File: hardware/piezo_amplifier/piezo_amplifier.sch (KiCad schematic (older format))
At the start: 4 parts

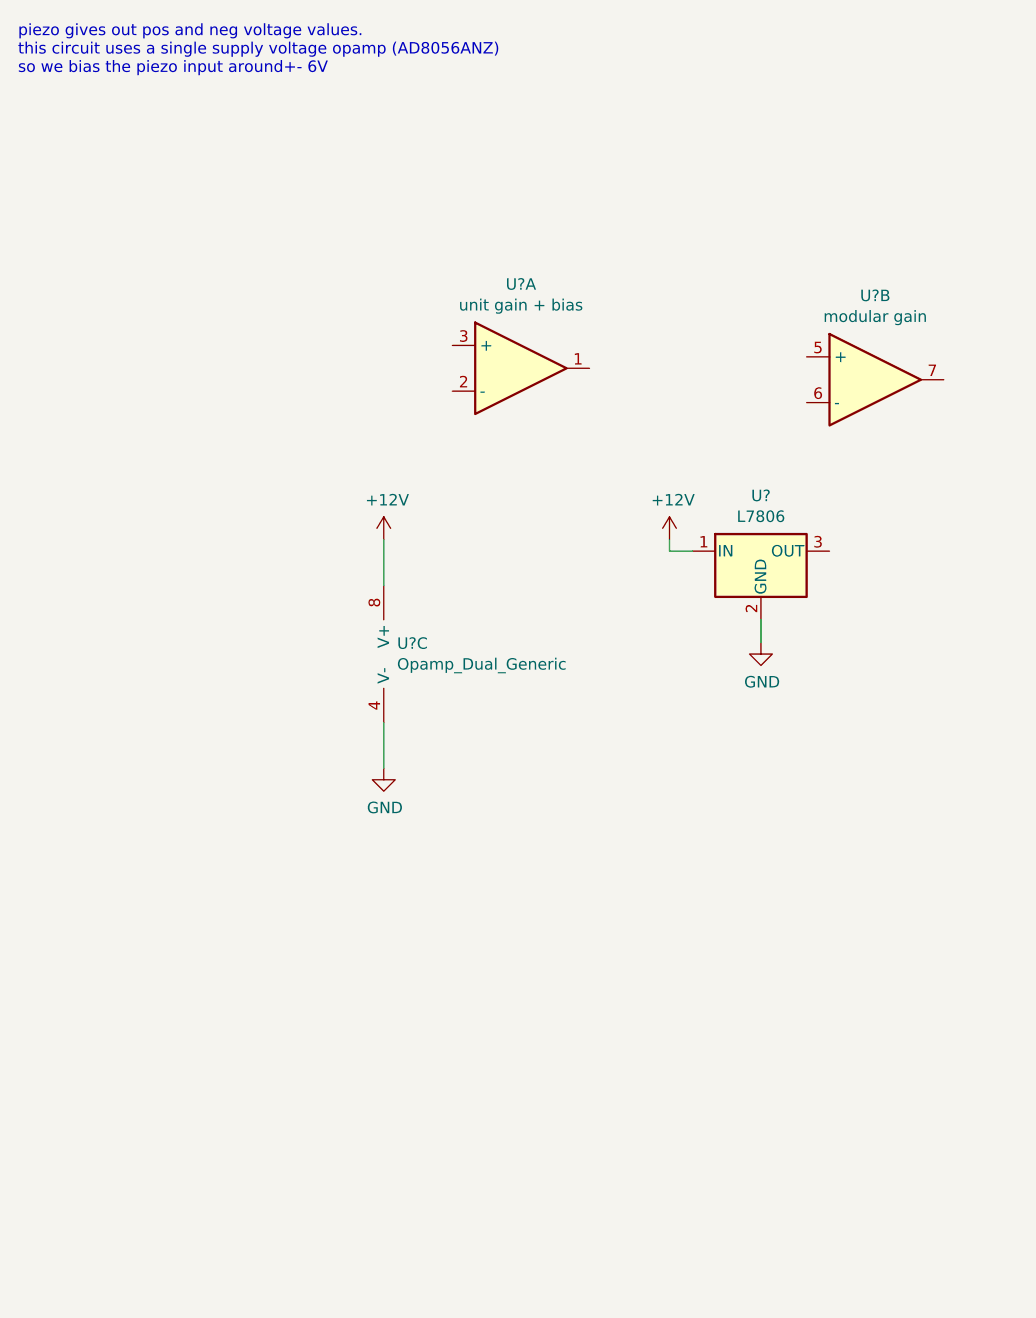
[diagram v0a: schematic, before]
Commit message: prototype zero for piezo amplifier
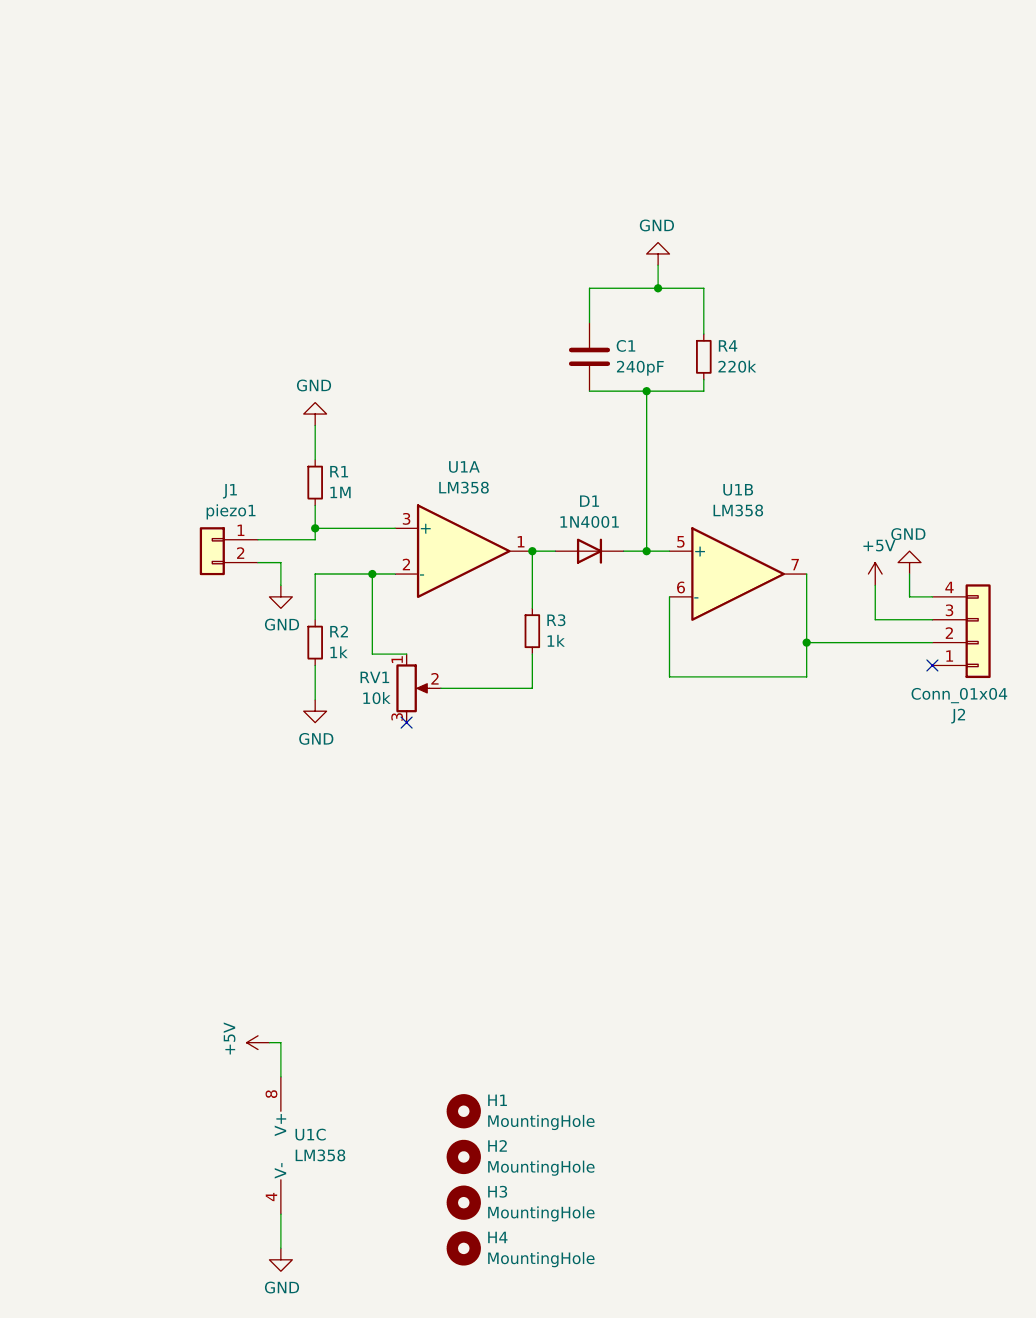
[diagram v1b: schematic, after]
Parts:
- removed U?: unit gain + bias, symbol Device:Opamp_Dual_Generic
- removed U?: modular gain, symbol Device:Opamp_Dual_Generic
- removed U?: Opamp_Dual_Generic, symbol Device:Opamp_Dual_Generic
- removed U?: L7806, symbol Regulator_Linear:L7806
- added C1: 240pF, Capacitor_THT:C_Disc_D4.7mm_W2.5mm_P5.00mm, symbol Device:C
- added D1: 1N4001, Diode_THT:D_DO-41_SOD81_P10.16mm_Horizontal, symbol Diode:1N4001
- added H1, H2, H3, H4: MountingHole, MountingHole:MountingHole_3.2mm_M3_ISO7380, symbol Mechanical:MountingHole
- added J1: piezo1, Connector_JST:JST_XH_B2B-XH-A_1x02_P2.50mm_Vertical, symbol Connector_Generic:Conn_01x02
- added J2: Conn_01x04, Connector_JST:JST_XH_B4B-XH-A_1x04_P2.50mm_Vertical, symbol Connector_Generic:Conn_01x04
- added R1: 1M, Resistor_THT:R_Axial_DIN0204_L3.6mm_D1.6mm_P5.08mm_Vertical, symbol Device:R_Small
- added R2, R3: 1k, Resistor_THT:R_Axial_DIN0204_L3.6mm_D1.6mm_P5.08mm_Vertical, symbol Device:R_Small
- added R4: 220k, Resistor_THT:R_Axial_DIN0204_L3.6mm_D1.6mm_P5.08mm_Vertical, symbol Device:R_Small
- added RV1: 10k, Connector_JST:JST_XH_B3B-XH-A_1x03_P2.50mm_Vertical, symbol Device:R_POT
- added U1: LM358, Package_DIP:DIP-8_W7.62mm_LongPads, symbol Amplifier_Operational:LM358
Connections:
- net GND: now also C1.1, J1.2 (Pin_2), J2.4 (Pin_4), R1.1, R2.2, R4.1, U1.4 (V-)
- new net: D1.2 (A), R3.1, U1.1
- new net: R2.1, RV1.1, U1.2 (-)
- new net: J1.1 (Pin_1), R1.2, U1.3 (+)
- new net: C1.2, D1.1 (K), R4.2, U1.5 (+)
- new net: J2.2 (Pin_2), U1.6 (-), U1.7
- new net: R3.2, RV1.2
- new net +5V: J2.3 (Pin_3), U1.8 (V+)
- no-connect marks 0 -> 2
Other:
- note removed: "piezo gives out pos and neg voltage values. \nthis circuit uses a single supply voltage opamp (AD8056ANZ)\nso we bias the piezo input around+- 6V\n\n"
